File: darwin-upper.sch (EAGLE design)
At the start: 50 parts, among them U1 TC58CVG1S3HRAIG, U2 TC58CVG1S3HRAIG, U3 TC58CVG1S3HRAIG, U4 TC58CVG1S3HRAIG

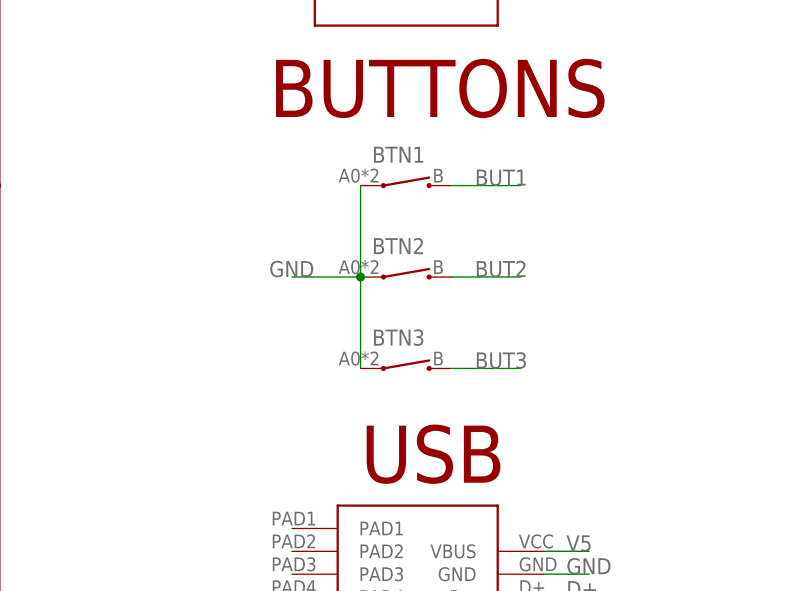
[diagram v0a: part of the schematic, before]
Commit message: Moved USB connector location, replaced buttons, tidied decoupling caps and routing.
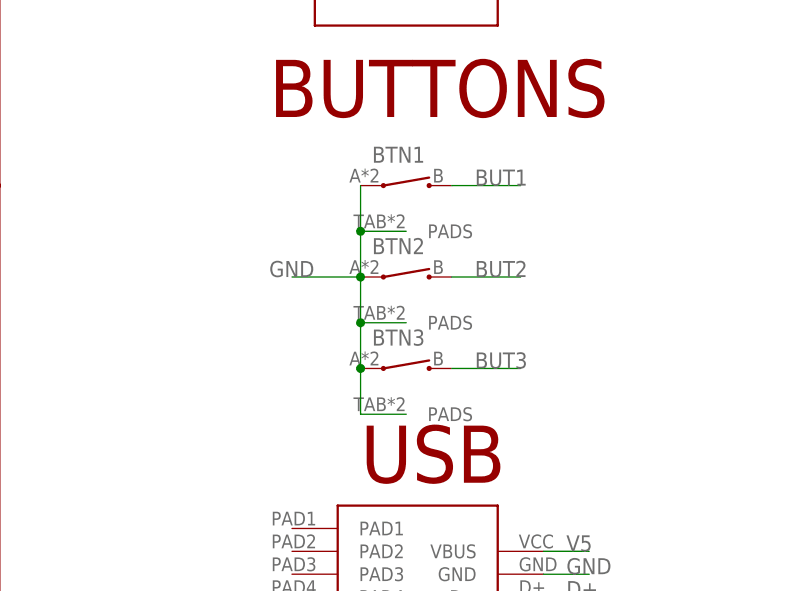
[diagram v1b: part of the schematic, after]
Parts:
- BTN1, BTN2, BTN3: value EVP-AEJB2A -> SKRTLAE010; device Conservify:EVP-AEJB2A -> Conservify:SKRTLAE010
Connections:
- net GND: now also BTN1.PADS, BTN2.PADS, BTN3.PADS
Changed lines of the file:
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@@
 <part name="UPPER" library="Conservify" library_urn="urn:adsk.eagle:library:11839183" deviceset="MOLEX-15-91-2200" device="F" package3d_urn="urn:adsk.eagle:package:11853535/2" value="MOLEX-15-91-2200F"/>
 <part name="LOWER" library="Conservify" library_urn="urn:adsk.eagle:library:11839183" deviceset="MOLEX-15-91-2200" device="F" package3d_urn="urn:adsk.eagle:package:11853535/2" value="MOLEX-15-91-2200F"/>
-<part name="BTN1" library="Conservify" library_urn="urn:adsk.eagle:library:11839183" deviceset="EVP-AEJB2A" device="" package3d_urn="urn:adsk.eagle:package:11839244/1"/>
-<part name="BTN2" library="Conservify" library_urn="urn:adsk.eagle:library:11839183" deviceset="EVP-AEJB2A" device="" package3d_urn="urn:adsk.eagle:package:11839244/1"/>
-<part name="BTN3" library="Conservify" library_urn="urn:adsk.eagle:library:11839183" deviceset="EVP-AEJB2A" device="" package3d_urn="urn:adsk.eagle:package:11839244/1"/>
+<part name="BTN1" library="Conservify" library_urn="urn:adsk.eagle:library:11839183" deviceset="SKRTLAE010" device="" package3d_urn="urn:adsk.eagle:package:15671107/2"/>
+<part name="BTN2" library="Conservify" library_urn="urn:adsk.eagle:library:11839183" deviceset="SKRTLAE010" device="" package3d_urn="urn:adsk.eagle:package:15671107/2"/>
+<part name="BTN3" library="Conservify" library_urn="urn:adsk.eagle:library:11839183" deviceset="SKRTLAE010" device="" package3d_urn="urn:adsk.eagle:package:15671107/2"/>
 <part name="U$14" library="Conservify" library_urn="urn:adsk.eagle:library:11839183" deviceset="ABS07W" device="" package3d_urn="urn:adsk.eagle:package:11839243/1"/>
 <part name="UTEMP" library="Conservify" library_urn="urn:adsk.eagle:library:11839183" deviceset="PCT2075" device="" package3d_urn="urn:adsk.eagle:package:11214694/2"/>
@@
 <pinref part="BTN1" gate="G$1" pin="1"/>
 <pinref part="BTN2" gate="G$1" pin="1"/>
-<wire x1="241.3" y1="0" x2="241.3" y2="-10.16" width="0.1524" layer="91"/>
+<wire x1="241.3" y1="0" x2="241.3" y2="-5.08" width="0.1524" layer="91"/>
 <pinref part="BTN3" gate="G$1" pin="1"/>
-<wire x1="241.3" y1="-20.32" x2="241.3" y2="-10.16" width="0.1524" layer="91"/>
+<wire x1="241.3" y1="-5.08" x2="241.3" y2="-10.16" width="0.1524" layer="91"/>
+<wire x1="241.3" y1="-20.32" x2="241.3" y2="-15.24" width="0.1524" layer="91"/>
 <junction x="241.3" y="-10.16"/>
+<wire x1="241.3" y1="-15.24" x2="241.3" y2="-10.16" width="0.1524" layer="91"/>
 <wire x1="241.3" y1="-10.16" x2="233.68" y2="-10.16" width="0.1524" layer="91"/>
 <label x="231.14" y="-10.16" size="1.778" layer="95"/>
-</segment>
-<segment>
+<pinref part="BTN3" gate="G$1" pin="PADS"/>
+<wire x1="246.38" y1="-25.4" x2="241.3" y2="-25.4" width="0.1524" layer="91"/>
+<wire x1="241.3" y1="-25.4" x2="241.3" y2="-20.32" width="0.1524" layer="91"/>
+<junction x="241.3" y="-20.32"/>
+<pinref part="BTN2" gate="G$1" pin="PADS"/>
+<wire x1="246.38" y1="-15.24" x2="241.3" y2="-15.24" width="0.1524" layer="91"/>
+<junction x="241.3" y="-15.24"/>
+<pinref part="BTN1" gate="G$1" pin="PADS"/>
+<wire x1="246.38" y1="-5.08" x2="241.3" y2="-5.08" width="0.1524" layer="91"/>
+<junction x="241.3" y="-5.08"/>
+</segment>
+<segment>

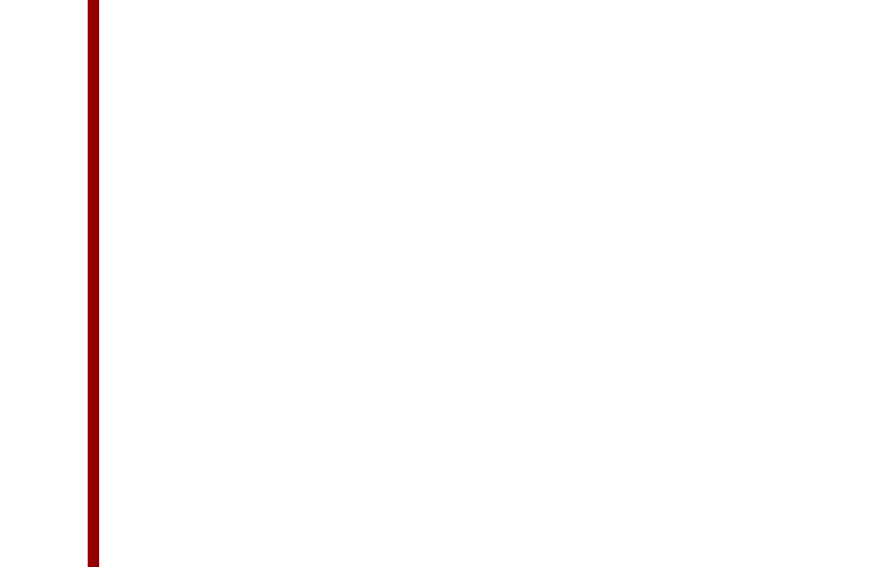
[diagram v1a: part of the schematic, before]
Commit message: Added Tag-Connect header.
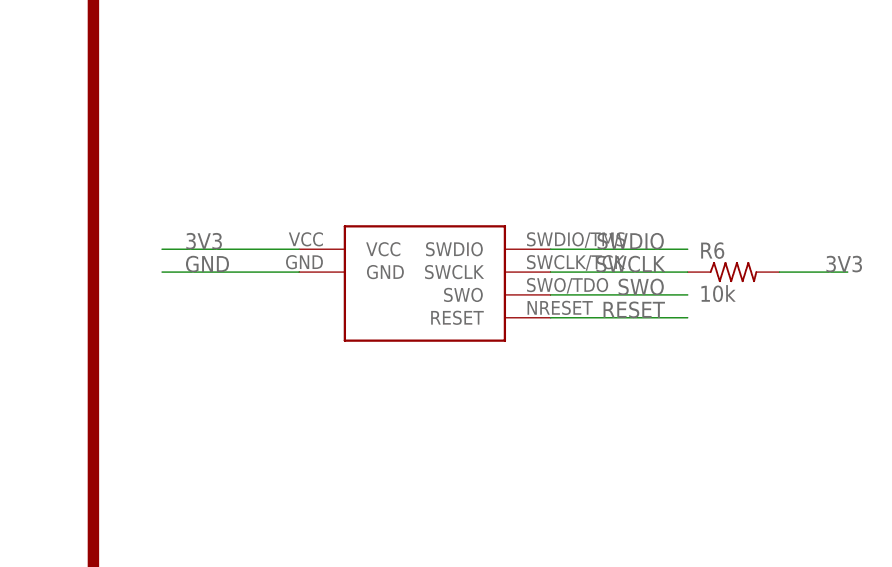
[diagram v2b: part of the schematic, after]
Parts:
- added J1: TAG-CONNECT, Conservify:TAG-CONNECT
- added R6: 10k, rcl:R-US_R0603
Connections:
- new net SWO: J1.SWO
- net 3V3: now also J1.VCC, R6.2
- net GND: now also J1.GND
- net RESET: now also J1.RESET
- net SWCLK: now also J1.SWCLK, R6.1
- net SWDIO: now also J1.SWDIO
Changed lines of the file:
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@@
 <?xml version="1.0" encoding="utf-8"?>
 <!DOCTYPE eagle SYSTEM "eagle.dtd">
-<eagle version="9.5.0">
+<eagle version="9.5.2">
 <drawing>
 <settings>
-<setting alwaysvectorfont="yes"/>
+<setting alwaysvectorfont="no"/>
 <setting verticaltext="up"/>
 </settings>
@@
 <part name="FID5" library="microbuilder" deviceset="FIDUCIAL" device="_1MM"/>
 <part name="FID6" library="microbuilder" deviceset="FIDUCIAL" device="_1MM"/>
+<part name="J1" library="Conservify" library_urn="urn:adsk.eagle:library:11839183" deviceset="TAG-CONNECT" device="" package3d_urn="urn:adsk.eagle:package:16969550/1"/>
+<part name="R6" library="rcl" library_urn="urn:adsk.eagle:library:334" deviceset="R-US_" device="R0603" package3d_urn="urn:adsk.eagle:package:23555/3" value="10k"/>
 </parts>
 <sheets>
@@
 <instance part="FID5" gate="G$1" x="307.34" y="-121.92" smashed="yes"/>
 <instance part="FID6" gate="G$1" x="307.34" y="-127" smashed="yes"/>
+<instance part="J1" gate="G$1" x="330.2" y="-27.94" smashed="yes"/>
+<instance part="R6" gate="G$1" x="365.76" y="-27.94" smashed="yes">
+<attribute name="NAME" x="361.95" y="-26.4414" size="1.778" layer="95"/>
+<attribute name="VALUE" x="361.95" y="-31.242" size="1.778" layer="96"/>
+</instance>
 </instances>
 <busses>
@@
 <label x="213.36" y="81.28" size="1.778" layer="95"/>
 </segment>
+<segment>
+<pinref part="J1" gate="G$1" pin="SWCLK"/>
+<wire x1="345.44" y1="-27.94" x2="360.68" y2="-27.94" width="0.1524" layer="91"/>
+<label x="358.14" y="-27.94" size="1.778" layer="95" align="bottom-right"/>
+<pinref part="R6" gate="G$1" pin="1"/>
+</segment>
 </net>
 <net name="SWDIO" class="0">
@@
 <wire x1="261.62" y1="81.28" x2="281.94" y2="81.28" width="0.1524" layer="91"/>
 <label x="279.4" y="81.28" size="1.778" layer="95" align="bottom-right"/>
+</segment>
+<segment>
+<pinref part="J1" gate="G$1" pin="SWDIO"/>
+<wire x1="345.44" y1="-25.4" x2="360.68" y2="-25.4" width="0.1524" layer="91"/>
+<label x="358.14" y="-25.4" size="1.778" layer="95" align="bottom-right"/>
 </segment>
 </net>
@@
 <label x="271.78" y="-91.44" size="1.778" layer="95"/>
 </segment>
+<segment>
+<pinref part="J1" gate="G$1" pin="GND"/>
+<wire x1="317.5" y1="-27.94" x2="302.26" y2="-27.94" width="0.1524" layer="91"/>
+<label x="304.8" y="-27.94" size="1.778" layer="95"/>
+</segment>
 </net>
 <net name="3V3" class="0">
@@
 <label x="271.78" y="-93.98" size="1.778" layer="95"/>
 </segment>
+<segment>
+<pinref part="J1" gate="G$1" pin="VCC"/>
+<wire x1="317.5" y1="-25.4" x2="302.26" y2="-25.4" width="0.1524" layer="91"/>
+<label x="304.8" y="-25.4" size="1.778" layer="95"/>
+</segment>
+<segment>
+<pinref part="R6" gate="G$1" pin="2"/>
+<wire x1="370.84" y1="-27.94" x2="378.46" y2="-27.94" width="0.1524" layer="91"/>
+<label x="375.92" y="-27.94" size="1.778" layer="95"/>
+</segment>
 </net>
 <net name="VBACKUP" class="0">
@@
 <label x="213.36" y="66.04" size="1.778" layer="95"/>
 </segment>
+<segment>
+<pinref part="J1" gate="G$1" pin="RESET"/>
+<wire x1="345.44" y1="-33.02" x2="360.68" y2="-33.02" width="0.1524" layer="91"/>
+<label x="358.14" y="-33.02" size="1.778" layer="95" align="bottom-right"/>
+</segment>
 </net>
 <net name="N$6" class="0">
@@
 </segment>
 </net>
+<net name="SWO" class="0">
+<segment>
+<pinref part="J1" gate="G$1" pin="SWO"/>
+<wire x1="345.44" y1="-30.48" x2="360.68" y2="-30.48" width="0.1524" layer="91"/>
+<label x="358.14" y="-30.48" size="1.778" layer="95" align="bottom-right"/>
+</segment>
+</net>

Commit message: Schematic cleanup and add PDF.
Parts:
- removed U$14: ABS07W, Conservify:ABS07W
- added XTAL: ABS07W, Conservify:ABS07W
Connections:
- net N$3: now also XTAL.2; no longer U$14.2
- net N$4: now also XTAL.1; no longer U$14.1
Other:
- note added: "PROGRAMMING HEADER"
- note added: "SCREEN"
- note removed: "CONN"
- moved on the sheet: BTN1, BTN2, BTN3, C23, C6, C7, D1, FLASH, LOWER, R1, R2, R3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
